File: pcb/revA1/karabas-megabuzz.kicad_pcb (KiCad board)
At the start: 4 copper layers, 92.2 x 44 mm, 175 parts, among them J1 FPGA JTAG, J2 Conn_02x31_Row_Letter_First, J3 uSD card, J4 PJ307, J5 Conn_01x04, J6 PRG, J7 NMI, SW1 SW_DIP_x05, T1 TestPoint1, T10 TestPoint2, T11 TestPoint2, T12 TestPoint2, T2 TestPoint2, T3 TestPoint, T4 TestPoint, T5 TestPoint, T6 TestPoint, T7 TestPoint, T8 TestPoint, T9 TestPoint2, U1 XC6SLX25-FTG256, U10 YMF262-M, U11 SAM2695, U12 PCM5102A, U13 PCM1808PWR, U14 CY62167EV30LL, U15 1117-3.3, U16 1117-3.3, U17 1117-1.2, U18 APS6404L-3SQRx-SN, U2 W25Q128JVS, U3 74AHCT1G125DB, U4 74AHCT1G125DB, U5 SN74CB3T3245PW, U6 SN74CB3T3245PW, U7 SN74CB3T3245PW, U8 SN74CB3T3245PW, U9 SN74LV1T34DBV, X1 50 MHz

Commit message: Fixed ROM block signal: swapped CSR / RDR
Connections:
- net Net-(J2-Pin_a13) renamed /Interfaces/~{BUS_IORQGE}
- J2 pad a15: unconnected-(J2-Pin_a15-Pada15) -> /Interfaces/~{BUS_RDR}
- J2 pad a25: Net-(J2-Pin_a25) -> unconnected-(J2-Pin_a25-Pada25)
- U4 pad 4: Net-(J2-Pin_a25) -> /Interfaces/~{BUS_RDR}
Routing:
- net /Interfaces/~{BUS_RDR}: track 0.00 -> 30.1 mm, vias 0 -> 2
- net Net-(J2-Pin_a25): track 7.99 -> 0.00 mm, vias 2 -> 0

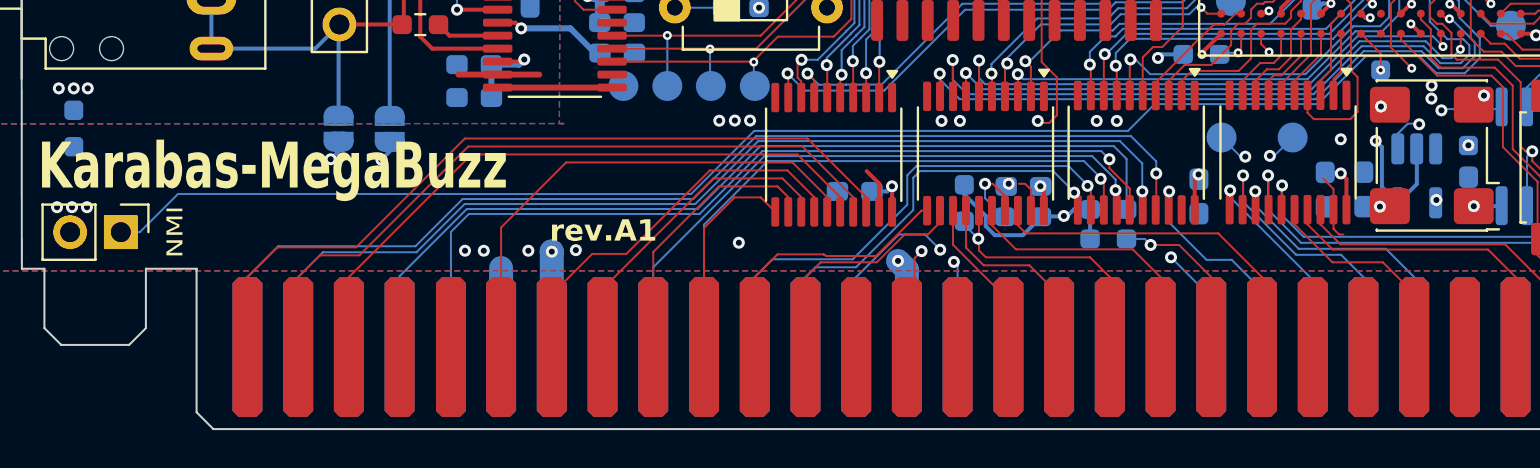
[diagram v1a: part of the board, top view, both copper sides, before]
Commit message: DivMMC + ZC for revA1 (#1)
* Current Divmmc WIP

* Added zx rom, fixed divmmc port decoding

* Fixed A1 Schematics / PCB with RDR + BLK signals

* Fixed divmmc by areset

* WIP

* Working 64kb divmmc + GS rom via flash loader

* removed zc_busy

* Project file update for 25k fpga

* Build files for 25k

* Fixed project for revA 16k

* Fixed project for revA 25k

* Added synth macros HW_A1

* Added synth macros HW_A1
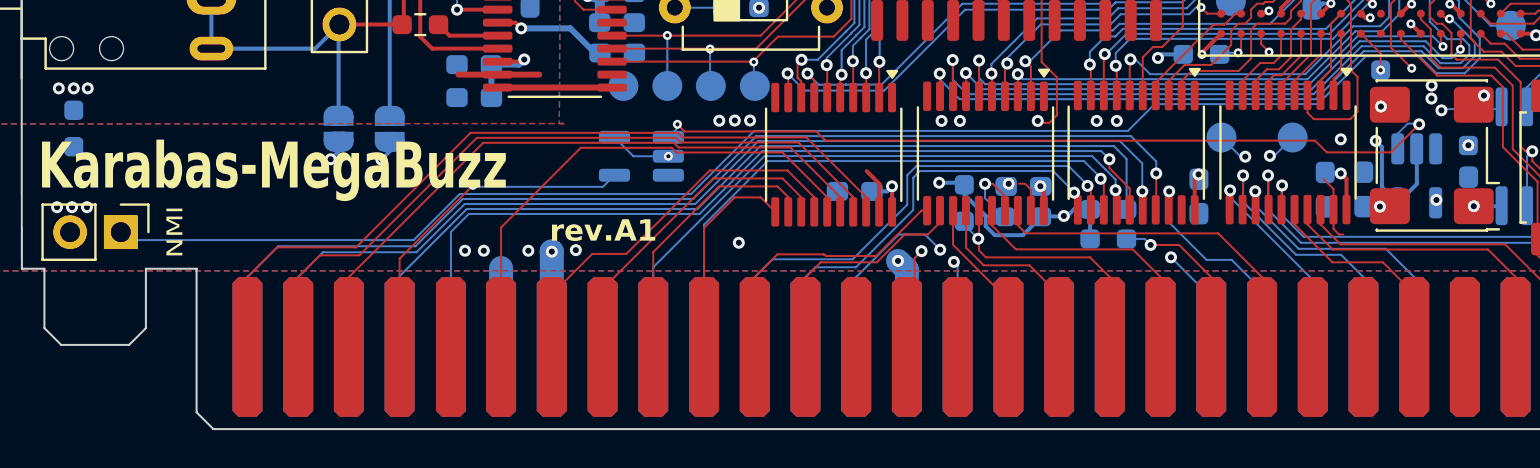
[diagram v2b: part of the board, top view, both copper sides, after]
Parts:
- added U19: 74AHCT1G125DB, Package_TO_SOT_SMD:SOT-23-5_HandSoldering, B.Cu at (128.4, 121.9)
- moved LOGO1 11.8 mm to (113.7, 123.3)
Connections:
- J2 pad b4: unconnected-(J2-Pin_b4-Padb4) -> /Interfaces/~{BUS_BLK}
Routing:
- net ~{ROMCS}: track 12.5 -> 51.6 mm, vias 2 -> 3
- net +5V: track 201.3 -> 219.8 mm, vias 18 -> 20
- net /Interfaces/~{BUS_BLK}: track 0.00 -> 17.0 mm, vias 0 -> 1
- net D0: track 25.1 -> 25.7 mm
